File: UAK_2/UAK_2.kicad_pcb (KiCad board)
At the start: 2 copper layers, 100 x 90 mm, 73 parts, among them K1 Кнопка_FSMSM, K2 Кнопка_FSMSM, X1 Крепежное_отверстие_М3, X2 Крепежное_отверстие_М3, X3 Крепежное_отверстие_М3, X4 Крепежное_отверстие_М3

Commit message: UAK.2A.MN + PDF +STEP
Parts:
- added HL2: TFT-дисплей_ST7735_ILI9341, N_VD_HL:TFT_2.8_INCH, F.Cu at (82.0, 96.2)
- HL1: footprint N_VD_HL:ЖК_MT-16S2H -> N_VD_HL:ЖК_MT-16S2H_2DRL
- moved G2 9.28 mm to (89.2, 107.0)
- moved VD3 9.10 mm to (94.2, 93.8)
- moved C12 7.32 mm to (89.5, 115.0)
- moved XP1 7.32 mm to (82.0, 85.8)
- moved RP1 2.25 mm to (77.8, 122.4)
- moved R1 2.00 mm to (135.5, 132.5)
- moved R4 2.00 mm to (138.8, 135.5)
- moved VT1 2.00 mm to (139.5, 131.2)
- moved HL1 1.45 mm to (88.5, 135.0)
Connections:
- A1 pad 14: Net-(A1-Pad14) -> /TFT_RES
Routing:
- net /MOSI: track 0.00 -> 83.1 mm, vias 0 -> 1
- net /LCD_LED: track 81.2 -> 146.9 mm, vias 2 -> 6
- net /LCD_E: track 118.3 -> 164.5 mm, vias 2 -> 3
- net /LCD_DATA_5: track 133.1 -> 177.0 mm, vias 2 -> 3
- net /LCD_A0: track 116.8 -> 159.9 mm, vias 2 -> 3
- net /GND: track 168.8 -> 209.7 mm, vias 24 -> 32
- net /LCD_DATA_6: track 136.7 -> 175.6 mm, vias 2 -> 3
- net /LCD_DATA_4: track 130.5 -> 169.3 mm, vias 2 -> 3
- net /TFT_RES: track 0.00 -> 38.0 mm, vias 0 -> 1
- net /LCD_DATA_7: track 137.1 -> 165.4 mm, vias 2 -> 3
- net Net-(VD3-Pad1): track 7.81 -> 19.6 mm, vias 0 -> 1
- net /5V: track 364.3 -> 372.8 mm
- net /BOOT_UART_RX: track 42.2 -> 48.3 mm
- net /BOOT_UART_TX: track 37.3 -> 43.1 mm
- net Net-(HL1-Pad3): track 49.6 -> 54.9 mm
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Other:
- board text added: "UAK.2A.MN"
- board text added: "XS2"
- board text removed: "UAK.1С.M9"

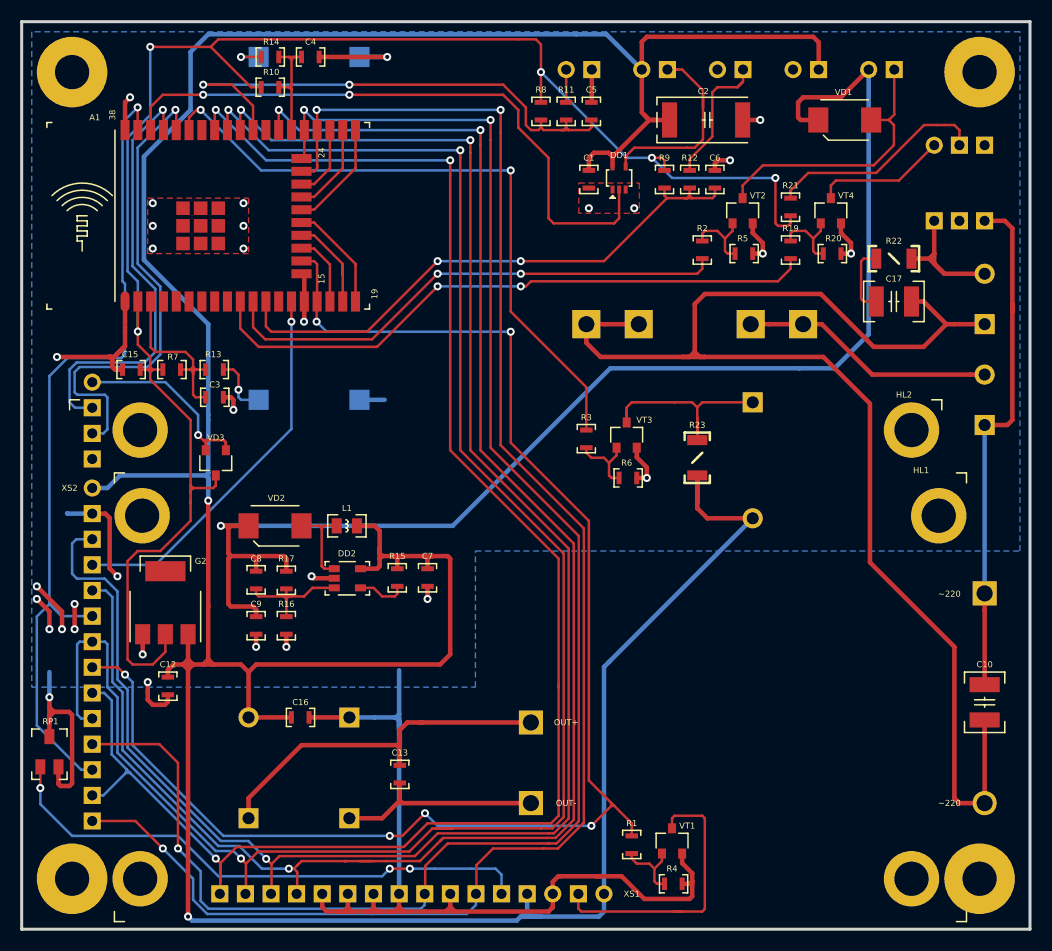
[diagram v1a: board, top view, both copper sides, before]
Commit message: заменен буфер, перекинуты ножки контроллера,, обновлены PCB +STEP +PDF
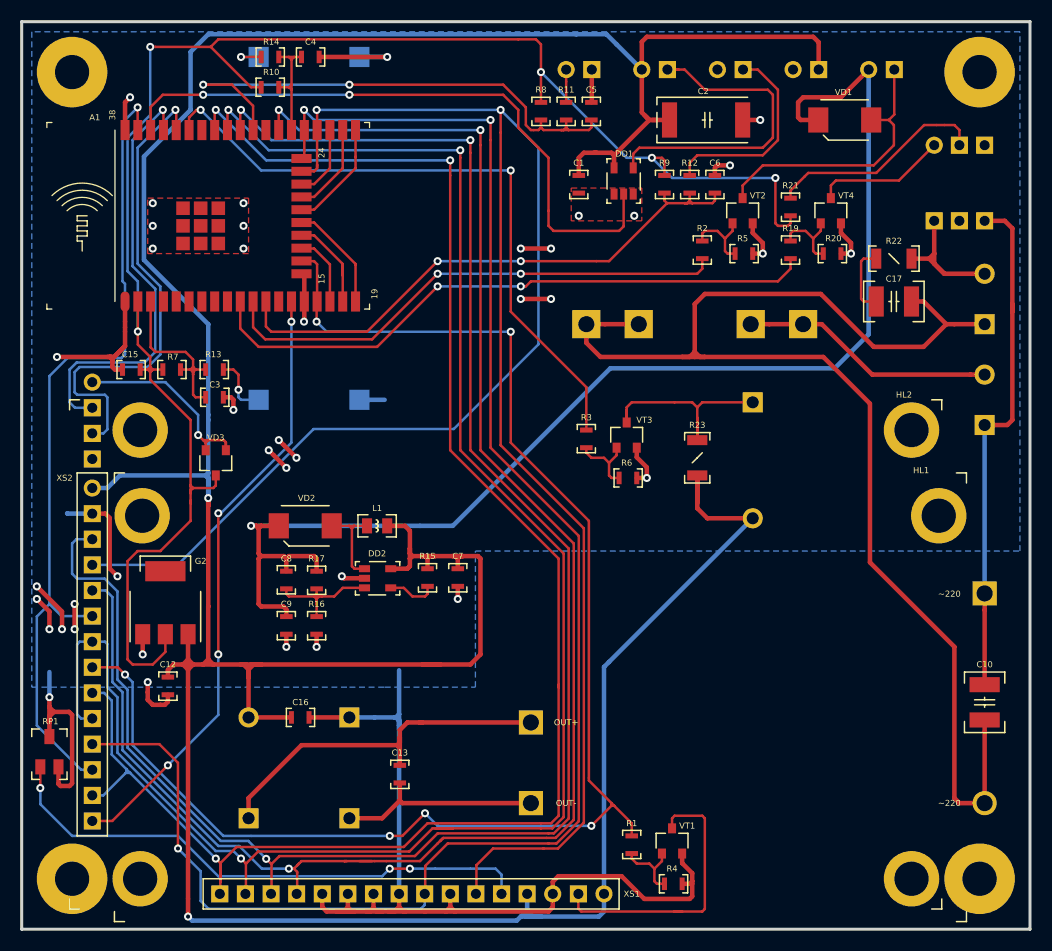
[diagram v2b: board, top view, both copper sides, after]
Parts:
- DD1: footprint N_DD:SC-70-5 -> N_G:Преобразователь_LM2703_SOT-23-5
- moved C7 3.00 mm to (118.2, 104.2)
- moved C8 3.00 mm to (101.2, 106.2)
- moved C9 3.00 mm to (101.2, 109.0)
- moved DD2 3.00 mm to (109.0, 104.2)
- moved L1 3.00 mm to (109.2, 100.0)
- moved R15 3.00 mm to (115.2, 104.2)
- moved R16 3.00 mm to (104.2, 109.0)
- moved R17 3.00 mm to (104.2, 104.5)
- moved VD2 3.00 mm to (105.5, 100.0)
- moved DD1 1.68 mm to (133.8, 67.1), turned to 0 degrees
- moved C1 1.12 mm to (130.2, 65.2)
- moved D1 1.00 mm to (113.8, 68.5)
- moved C6 0.50 mm to (143.8, 65.2)
- moved R12 0.50 mm to (141.2, 65.2)
- moved R9 0.50 mm to (138.8, 65.2)
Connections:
- A1 pad 14: /TFT_RES -> /TOUCH_IRQ
- HL2 pad 14: /LCD_A0 -> /TOUCH_IRQ
- HL2 pad 4: /TFT_RES -> /LCD_A0
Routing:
- net /TOUCH_IRQ: track 0.00 -> 61.0 mm, vias 0 -> 4
- net /TFT_RES: track 38.0 -> 0.00 mm, vias 1 -> 0
- net /LCD_A0: track 159.9 -> 193.4 mm, vias 3 -> 2
- net /5V: track 372.8 -> 385.4 mm
- net /LED_OUT: track 21.1 -> 32.8 mm
- net /GND: track 209.7 -> 220.7 mm, vias 32 -> 40
- net /BUTT_1: track 14.1 -> 20.2 mm
- net /12V: track 133.5 -> 130.5 mm
- net /LED_WS2812: track 62.1 -> 63.7 mm
- net /3V3: track 173.6 -> 174.1 mm
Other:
- board text added: "UAK.2B.MN"
- board text removed: "UAK.2A.MN"
